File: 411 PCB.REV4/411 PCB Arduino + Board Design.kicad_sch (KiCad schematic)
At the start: 37 parts, among them J1 ICSP CONN, J3 Conn_01x04, J4 Conn_01x05_Pin, Q1 Q_NMOS_GDS, SW1 SW_SPST, SW2 SW_MEC_5E, SW3 SW_DPDT_x2, SW4 SW_DPST_x2, U2 ATmega328P-P, Y1 8 MHz

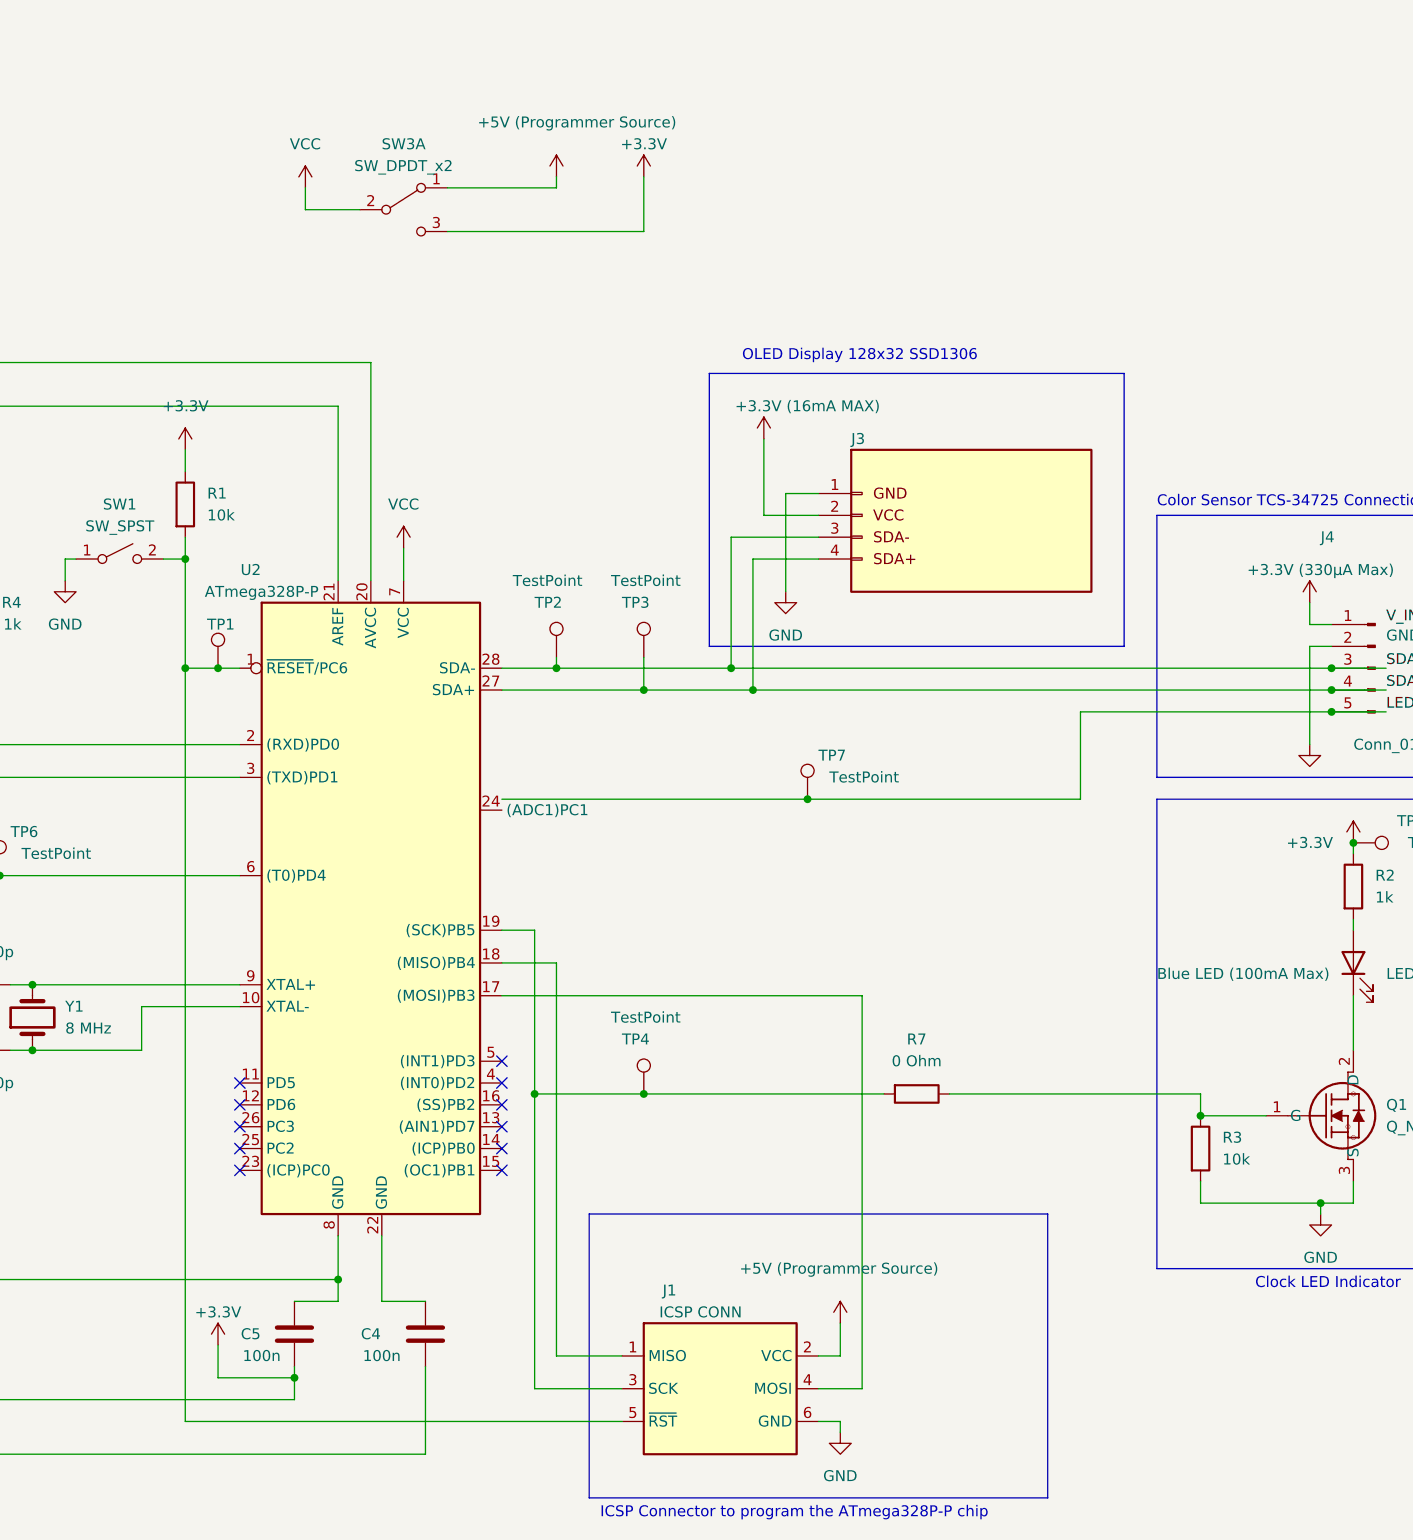
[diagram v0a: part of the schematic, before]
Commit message: PCB Layout REV 4
Updated Schematic and Layout (Added power switches, fixed Atmega pin out schematic, changed pin outputs on color sensor, added 3.3V to 5V throw select switch)
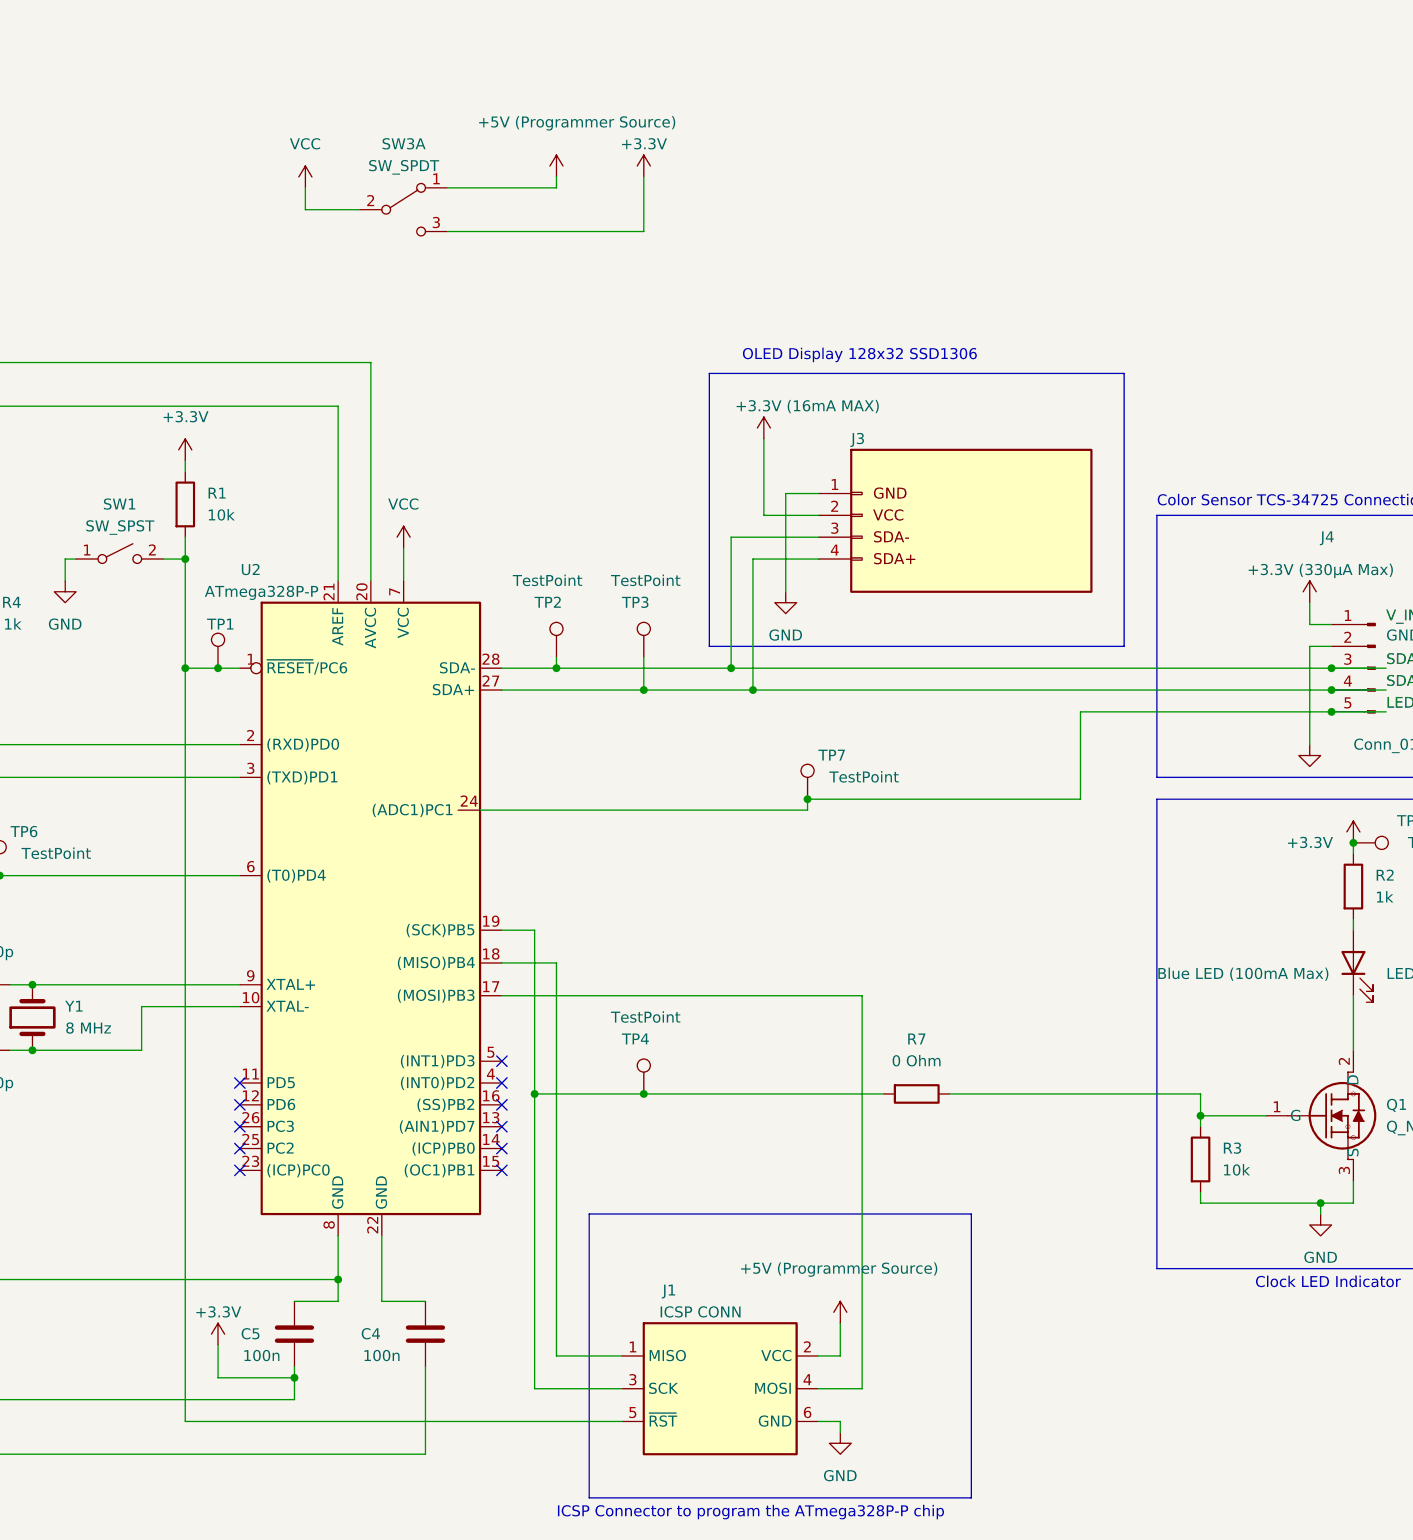
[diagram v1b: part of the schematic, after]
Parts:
- J4: footprint (none) -> Connector_PinHeader_2.54mm:PinHeader_1x05_P2.54mm_Vertical
- SW3: value SW_DPDT_x2 -> SW_SPDT; footprint (none) -> Button_Switch_THT:SW_E-Switch_EG1271_SPDT_123
- SW4: footprint (none) -> Button_Switch_THT:SW_DIP_SPSTx01_Slide_9.78x4.72mm_W7.62mm_P2.54mm
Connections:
- net LED_EN: now also U2.24 ((ADC1)PC1)
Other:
- moved on the sheet: R3, U2
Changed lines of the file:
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@@
     (stroke (width 0) (type default))
   )
-  (wire (pts (xy 298.45 204.47) (xy 334.01 204.47))
+  (wire (pts (xy 295.91 205.74) (xy 334.01 205.74))
     (stroke (width 0) (type default))
   )
@@
     (stroke (width 0) (type default))
   )
-  (wire (pts (xy 261.62 163.83) (xy 261.62 166.37))
+  (wire (pts (xy 261.62 165.1) (xy 261.62 166.37))
     (stroke (width 0) (type default))
   )
@@
     (stroke (width 0) (type default))
   )
+  (wire (pts (xy 334.01 205.74) (xy 334.01 204.47))
+    (stroke (width 0) (type default))
+  )
   (wire (pts (xy 232.41 233.68) (xy 232.41 238.76))
     (stroke (width 0) (type default))
@@
     (stroke (width 0) (type default))
   )
-  (wire (pts (xy 379.73 251.46) (xy 379.73 248.92))
+  (wire (pts (xy 379.73 251.46) (xy 379.73 250.19))
     (stroke (width 0) (type default))
   )
@@
     (stroke (width 0) (type default))
   )
-  (rectangle (start 308.61 252.73) (end 361.95 285.75)
+  (wire (pts (xy 379.73 242.57) (xy 379.73 241.3))
+    (stroke (width 0) (type default))
+  )
+  (rectangle (start 308.61 252.73) (end 353.06 285.75)
     (stroke (width 0) (type default))
     (fill (type none))
@@
     (effects (font (size 1.27 1.27)) (justify left bottom))
   )
-  (text "ICSP Connector to program the ATmega328P-P chip" (at 309.88 288.29 0)
+  (text "ICSP Connector to program the ATmega328P-P chip" (at 304.8 288.29 0)
     (effects (font (size 1.27 1.27)) (justify left bottom))
   )
@@
       (effects (font (size 1.27 1.27)))
     )
-    (property "Footprint" "" (at 111.76 99.06 0)
+    (property "Footprint" "Button_Switch_THT:SW_DIP_SPSTx01_Slide_9.78x4.72mm_W7.62mm_P2.54mm" (at 111.76 99.06 0)
       (effects (font (size 1.27 1.27)) hide)
     )
@@
       (effects (font (size 1.27 1.27)) (justify right))
     )
-    (property "Footprint" "" (at 400.05 189.23 0)
+    (property "Footprint" "Connector_PinHeader_2.54mm:PinHeader_1x05_P2.54mm_Vertical" (at 400.05 189.23 0)
       (effects (font (size 1.27 1.27)) hide)
     )
@@
     )
   )
-  (symbol (lib_id "Device:R") (at 379.73 245.11 0) (unit 1)
-    (in_bom yes) (on_board yes) (dnp no) (fields_autoplaced)
-    (property "Reference" "R3" (at 382.27 243.84 0)
-      (effects (font (size 1.27 1.27)) (justify left))
-    )
-    (property "Value" "10k" (at 382.27 246.38 0)
-      (effects (font (size 1.27 1.27)) (justify left))
-    )
-    (property "Footprint" "Resistor_SMD:R_1206_3216Metric" (at 377.952 245.11 90)
-      (effects (font (size 1.27 1.27)) hide)
-    )
-    (property "Datasheet" "~" (at 379.73 245.11 0)
+  (symbol (lib_id "Device:R") (at 379.73 246.38 0) (unit 1)
+    (in_bom yes) (on_board yes) (dnp no) (fields_autoplaced)
+    (property "Reference" "R3" (at 382.27 245.11 0)
+      (effects (font (size 1.27 1.27)) (justify left))
+    )
+    (property "Value" "10k" (at 382.27 247.65 0)
+      (effects (font (size 1.27 1.27)) (justify left))
+    )
+    (property "Footprint" "Resistor_SMD:R_1206_3216Metric" (at 377.952 246.38 90)
+      (effects (font (size 1.27 1.27)) hide)
+    )
+    (property "Datasheet" "~" (at 379.73 246.38 0)
       (effects (font (size 1.27 1.27)) hide)
     )
@@
     )
   )
-  (symbol (lib_id "power:+3.3V") (at 261.62 163.83 0) (unit 1)
-    (in_bom yes) (on_board yes) (dnp no) (fields_autoplaced)
-    (property "Reference" "#+3.3V0105" (at 261.62 167.64 0)
-      (effects (font (size 1.27 1.27)) hide)
-    )
-    (property "Value" "+3.3V" (at 261.62 158.75 0)
-      (effects (font (size 1.27 1.27)))
-    )
-    (property "Footprint" "" (at 261.62 163.83 0)
-      (effects (font (size 1.27 1.27)) hide)
-    )
-    (property "Datasheet" "" (at 261.62 163.83 0)
+  (symbol (lib_id "power:+3.3V") (at 261.62 165.1 0) (unit 1)
+    (in_bom yes) (on_board yes) (dnp no) (fields_autoplaced)
+    (property "Reference" "#+3.3V0105" (at 261.62 168.91 0)
+      (effects (font (size 1.27 1.27)) hide)
+    )
+    (property "Value" "+3.3V" (at 261.62 160.02 0)
+      (effects (font (size 1.27 1.27)))
+    )
+    (property "Footprint" "" (at 261.62 165.1 0)
+      (effects (font (size 1.27 1.27)) hide)
+    )
+    (property "Datasheet" "" (at 261.62 165.1 0)
       (effects (font (size 1.27 1.27)) hide)
     )
@@
       (effects (font (size 1.27 1.27)))
     )
-    (property "Value" "SW_DPDT_x2" (at 287.02 130.81 0)
-      (effects (font (size 1.27 1.27)))
-    )
-    (property "Footprint" "" (at 287.02 135.89 0)
-      (effects (font (size 1.27 1.27)) hide)
-    )
+    (property "Value" "SW_SPDT" (at 287.02 130.81 0)
+      (effects (font (size 1.27 1.27)))
+    )
+    (property "Footprint" "Button_Switch_THT:SW_E-Switch_EG1271_SPDT_123" (at 287.02 135.89 0)
+      (effects (font (size 1.27 1.27)) hide)
+    )
